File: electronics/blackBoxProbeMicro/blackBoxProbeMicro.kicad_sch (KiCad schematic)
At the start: 67 parts, among them J1 USB-C, J2 JTAG_2X05, J3 JTAG_2X05, J4 DevBoardUartOutput, Q1 BSD840N, Q2 NTJD4152P, U1 MCP1702-MB, U2 DT1446-04S, U3 STM32F103CBT, Y1 8MHz

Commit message: fixing ERC/DRC errors after component updates
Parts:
- H1, H2: symbol SquantorPCBOutline:Drill_Hole_no_metal -> Mechanical:MountingHole
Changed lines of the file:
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@@
     (stroke (width 0) (type default) (color 0 0 0 0))
   )
-  (wire (pts (xy 114.3 91.44) (xy 113.03 91.44))
+  (wire (pts (xy 110.49 91.44) (xy 114.3 91.44))
     (stroke (width 0) (type default) (color 0 0 0 0))
   )
@@
     (stroke (width 0) (type default) (color 0 0 0 0))
   )
-  (wire (pts (xy 99.06 91.44) (xy 100.33 91.44))
+  (wire (pts (xy 99.06 91.44) (xy 102.87 91.44))
     (stroke (width 0) (type default) (color 0 0 0 0))
   )
@@
     (pin "2")
   )
-  (symbol (lib_id "SquantorPCBOutline:Drill_Hole_no_metal") (at 38.1 187.96 0) (unit 1)
+  (symbol (lib_id "Mechanical:MountingHole") (at 38.1 187.96 0) (unit 1)
     (in_bom yes) (on_board yes)
     (property "Reference" "H2" (id 0) (at 42.6212 186.6138 0)
@@
     )
     (property "Footprint" "SquantorPcbOutline:MountingHole_2.5mm_no_metal" (id 2) (at 38.1 187.96 0)
-      (effects (font (size 1.524 1.524)) hide)
-    )
-    (property "Datasheet" "" (id 3) (at 38.1 187.96 0)
-      (effects (font (size 1.524 1.524)) hide)
-    )
-  )
-  (symbol (lib_id "SquantorPCBOutline:Drill_Hole_no_metal") (at 38.1 179.07 0) (unit 1)
+      (effects (font (size 1.27 1.27)) hide)
+    )
+    (property "Datasheet" "~" (id 3) (at 38.1 187.96 0)
+      (effects (font (size 1.27 1.27)) hide)
+    )
+  )
+  (symbol (lib_id "Mechanical:MountingHole") (at 38.1 179.07 0) (unit 1)
     (in_bom yes) (on_board yes)
     (property "Reference" "H1" (id 0) (at 42.6212 177.7238 0)
@@
     )
     (property "Footprint" "SquantorPcbOutline:MountingHole_2.5mm_no_metal" (id 2) (at 38.1 179.07 0)
-      (effects (font (size 1.524 1.524)) hide)
-    )
-    (property "Datasheet" "" (id 3) (at 38.1 179.07 0)
-      (effects (font (size 1.524 1.524)) hide)
-    )
-  )
+      (effects (font (size 1.27 1.27)) hide)
+    )
+    (property "Datasheet" "~" (id 3) (at 38.1 179.07 0)
+      (effects (font (size 1.27 1.27)) hide)
+    )
+  )

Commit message: small uppdates
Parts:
- N2: value V:20230224 -> V:20230929

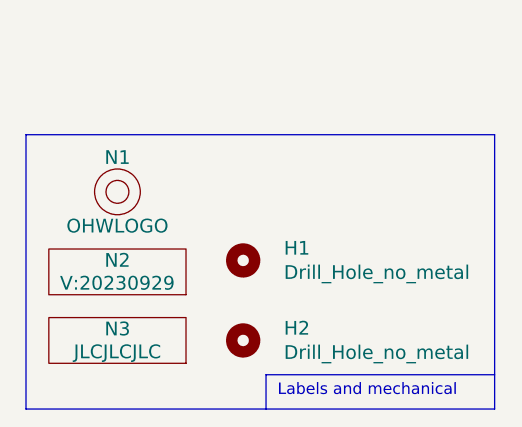
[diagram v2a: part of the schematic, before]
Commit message: WIP adapting to aisler DRC
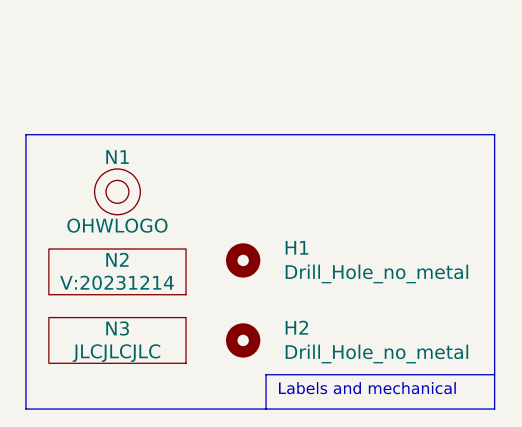
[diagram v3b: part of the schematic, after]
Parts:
- N2: value V:20230929 -> V:20231214
- U1: footprint SquantorIC:SOT89-NXP-Viatab -> SquantorIC:SOT89-NXP
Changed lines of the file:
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@@
       (effects (font (size 1.524 1.524)))
     )
-    (property "Footprint" "SquantorIC:SOT89-NXP-Viatab" (at 76.2 127 0)
+    (property "Footprint" "SquantorIC:SOT89-NXP" (at 76.2 127 0)
       (effects (font (size 1.524 1.524)) hide)
     )
@@
       (effects (font (size 1.524 1.524)))
     )
-    (property "Value" "V:20230929" (at 24.13 181.61 0)
-      (effects (font (size 1.524 1.524)))
-    )
+    (property "Value" "V:20231214" (at 24.13 181.61 0)
+      (effects (font (size 1.524 1.524)))
+    )

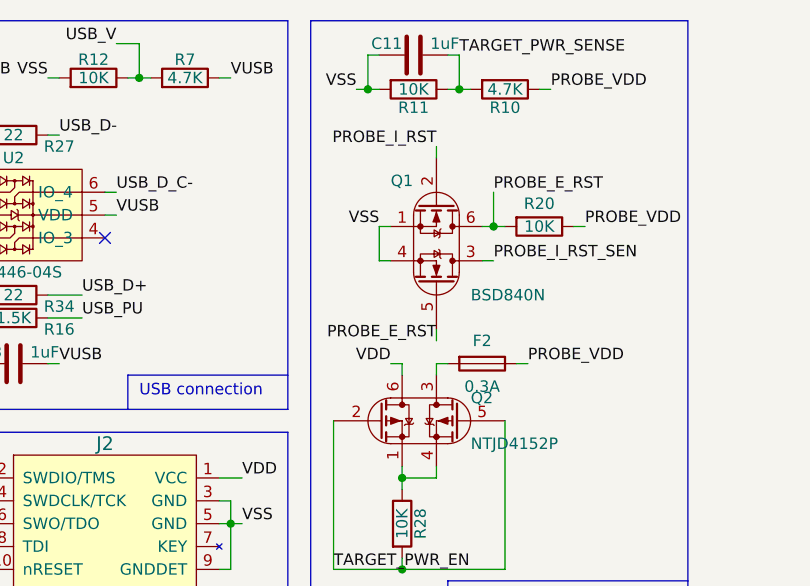
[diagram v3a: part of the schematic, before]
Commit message: WIP updating parts and PCB, replacing silk parts
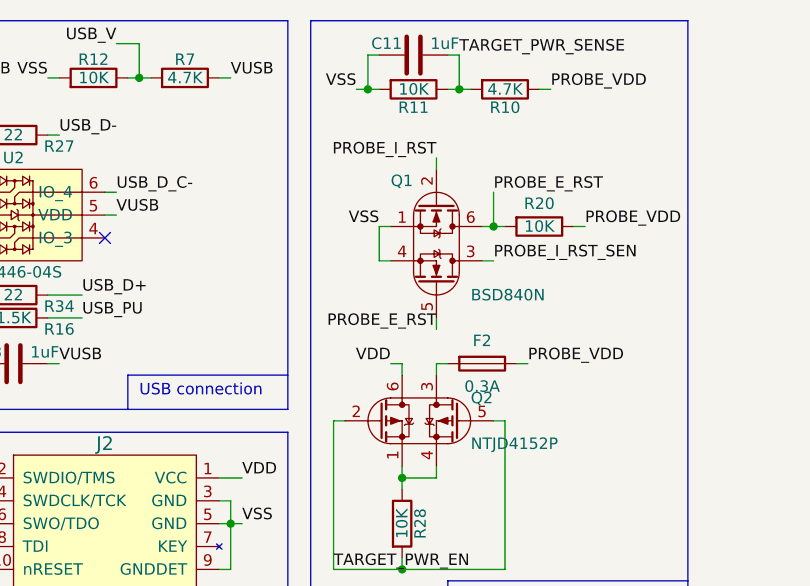
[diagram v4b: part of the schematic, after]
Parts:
- C1, C2, C4: footprint SquantorRcl:C_0603 -> SquantorCapacitor:C_0603
- C10, C11, C12, C13, C3, C5, C6, C7, C8: footprint SquantorRcl:C_0402 -> SquantorCapacitor:C_0402
- F1, F2: footprint SquantorRcl:F_0603_hand -> SquantorFuse:F_0603_hand
- FB1: footprint SquantorRcl:L_0603 -> SquantorInductor:L_0603
- FB2, FB3: footprint SquantorRcl:L_0402 -> SquantorInductor:L_0402
- J4: footprint Connector_JST:JST_PH_S4B-PH-K_1x04_P2.00mm_Horizontal -> SquantorConnectors:JST_PH_S4B-PH-K_1x04_P2.00mm_Horizontal
- R1, R10, R11, R12, R13, R14, R15, R16, R17, R18, R19, R2, R20, R21, R22, R23, R24, R25, R27, R28, R3, R34, R4, R5, R6, R7, R8, R9: footprint SquantorRcl:R_0402_hand -> SquantorResistor:R_0402_hand

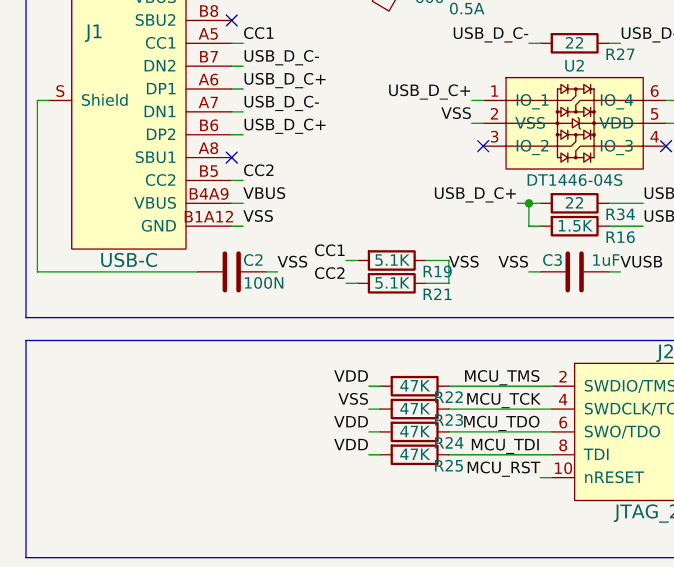
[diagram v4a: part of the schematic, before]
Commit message: WIP relayout on new DRC rules
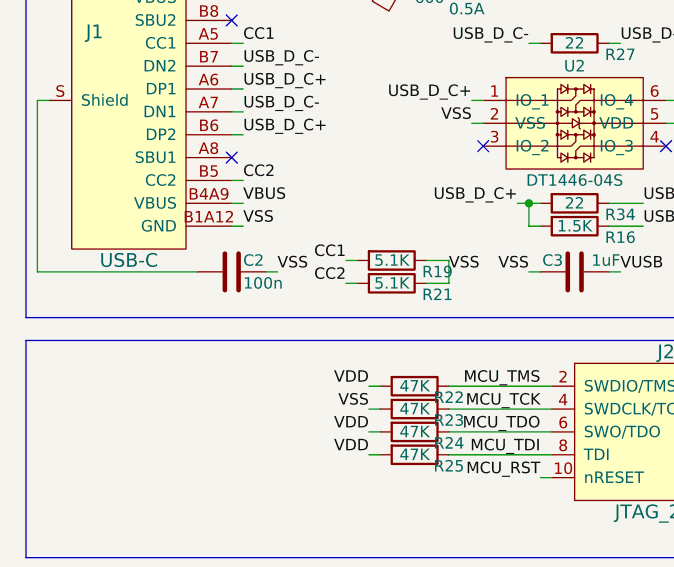
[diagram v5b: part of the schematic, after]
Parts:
- C2: value 100N -> 100n
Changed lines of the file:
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@@
       (effects (font (size 1.27 1.27)) (justify left))
     )
-    (property "Value" "100N" (at 38.1 53.34 90)
+    (property "Value" "100n" (at 38.1 53.34 90)
       (effects (font (size 1.27 1.27)) (justify left))
     )

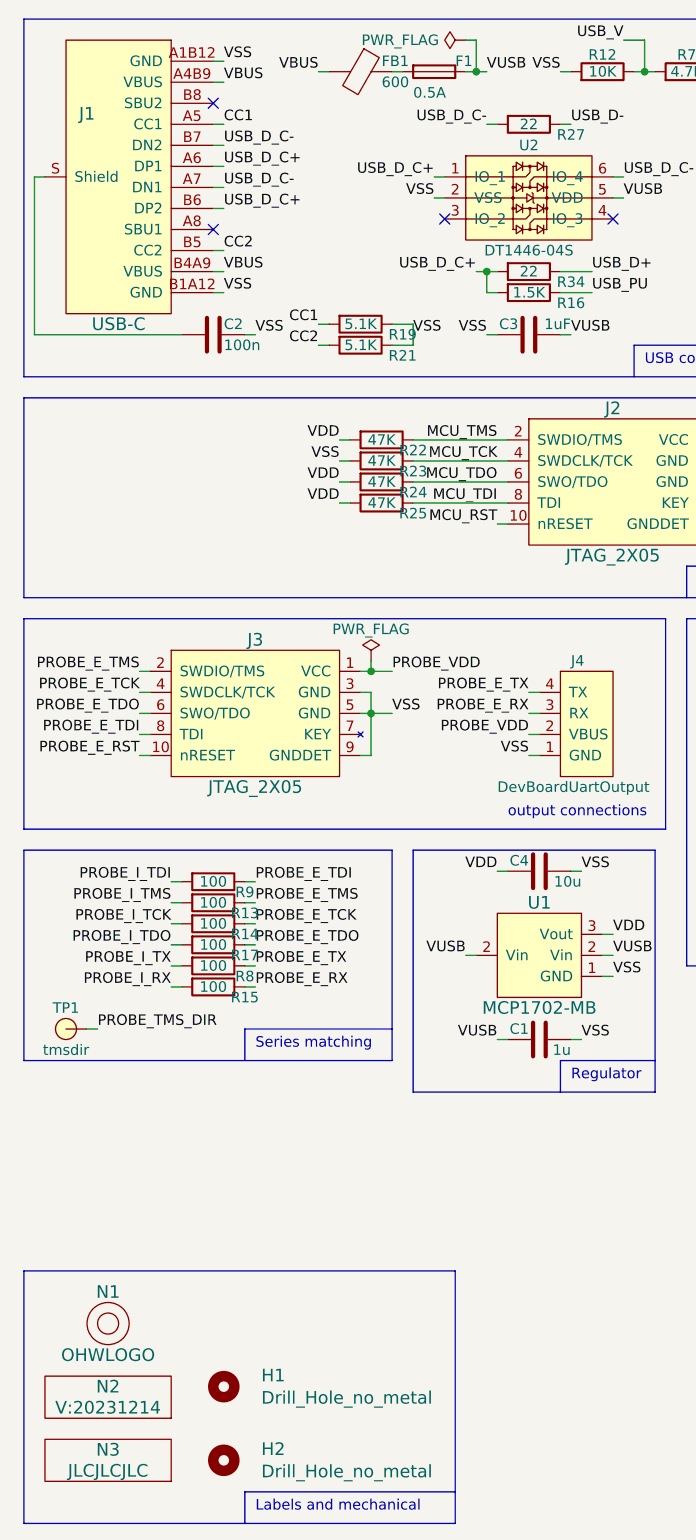
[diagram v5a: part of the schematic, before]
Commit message: adjustments of silk, fixing ERC errors
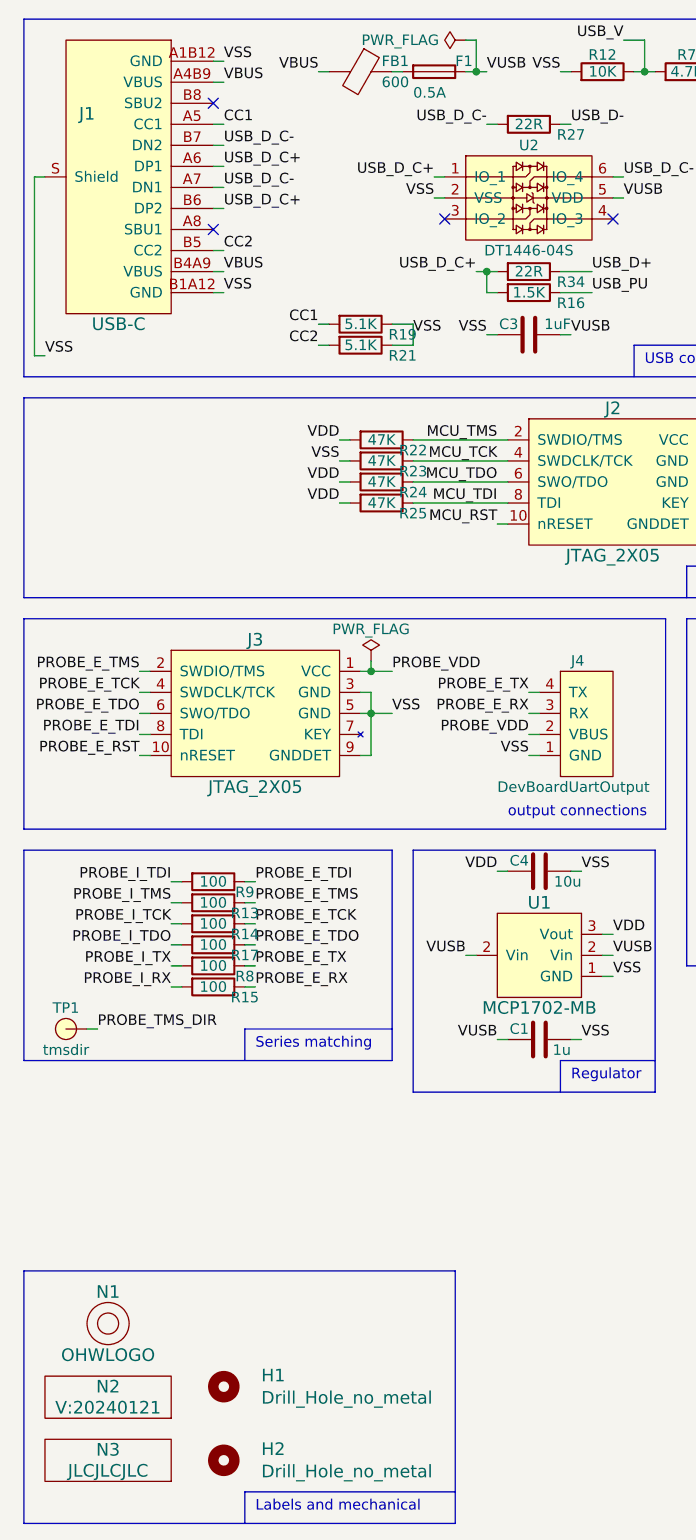
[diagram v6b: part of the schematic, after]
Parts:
- removed C2: 100n, SquantorCapacitor:C_0603, symbol Device:C
- N2: value V:20231214 -> V:20240121
- R27, R34: value 22 -> 22R
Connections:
- net VSS: now also J1.S (Shield)
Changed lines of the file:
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@@
-    (stroke (width 0) (type default))
-  )
-  (wire (pts (xy 33.02 52.07) (xy 15.24 52.07))
     (stroke (width 0) (type default))
   )
@@
     (stroke (width 0) (type default))
   )
-  (wire (pts (xy 15.24 52.07) (xy 15.24 33.02))
-    (stroke (width 0) (type default))
-  )
   (wire (pts (xy 227.33 39.37) (xy 226.06 39.37))
     (stroke (width 0) (type default))
@@
     (stroke (width 0) (type default))
   )
+  (wire (pts (xy 15.24 33.02) (xy 15.24 54.61))
+    (stroke (width 0) (type default))
+  )
   (polyline (pts (xy 105.41 59.69) (xy 105.41 83.82))
     (stroke (width 0) (type default))
@@
     (stroke (width 0) (type default))
   )
-  (wire (pts (xy 15.24 33.02) (xy 16.51 33.02))
-    (stroke (width 0) (type default))
-  )
   (wire (pts (xy 115.57 40.64) (xy 116.84 40.64))
     (stroke (width 0) (type default))
@@
     (stroke (width 0) (type default))
   )
-  (wire (pts (xy 40.64 52.07) (xy 41.91 52.07))
-    (stroke (width 0) (type default))
-  )
   (polyline (pts (xy 175.26 166.37) (xy 175.26 195.58))
     (stroke (width 0) (type default))
@@
     (stroke (width 0) (type default))
   )
+  (wire (pts (xy 16.51 33.02) (xy 15.24 33.02))
+    (stroke (width 0) (type default))
+  )
   (wire (pts (xy 72.39 74.93) (xy 71.12 74.93))
     (stroke (width 0) (type default))
@@
     (stroke (width 0) (type default))
   )
+  (wire (pts (xy 15.24 54.61) (xy 16.51 54.61))
+    (stroke (width 0) (type default))
+  )
   (polyline (pts (xy 184.15 160.02) (xy 283.21 160.02))
     (stroke (width 0) (type default))
@@
     (effects (font (size 1.27 1.27)) (justify right bottom))
   )
-  (label "VSS" (at 41.91 52.07 0) (fields_autoplaced)
+  (label "VSS" (at 16.51 54.61 0) (fields_autoplaced)
     (effects (font (size 1.27 1.27)) (justify left bottom))
   )
@@
         (path "/40f15b6a-8b98-4774-8d8e-1b991685cf13"
           (reference "J1") (unit 1)
-        )
-      )
-    )
-  )
-  (symbol (lib_id "Device:C") (at 36.83 52.07 270) (unit 1)
-    (in_bom yes) (on_board yes) (dnp no)
-    (property "Reference" "C2" (at 38.1 50.8 90)
-      (effects (font (size 1.27 1.27)) (justify left))
-    )
-    (property "Value" "100n" (at 38.1 53.34 90)
-      (effects (font (size 1.27 1.27)) (justify left))
-    )
-    (property "Footprint" "SquantorCapacitor:C_0603" (at 33.02 53.0352 0)
-      (effects (font (size 1.27 1.27)) hide)
-    )
-    (property "Datasheet" "~" (at 36.83 52.07 0)
-      (effects (font (size 1.27 1.27)) hide)
-    )
-    (pin "1")
-    (pin "2")
-    (instances
-      (project "blackBoxProbeMicro"
-        (path "/40f15b6a-8b98-4774-8d8e-1b991685cf13"
-          (reference "C2") (unit 1)
         )
       )
@@
       (effects (font (size 1.27 1.27)))
     )
-    (property "Value" "22" (at 74.93 26.67 90)
+    (property "Value" "22R" (at 74.93 26.67 90)
       (effects (font (size 1.27 1.27)))
     )
@@
       (effects (font (size 1.27 1.27)))
     )
-    (property "Value" "22" (at 74.93 44.45 90)
+    (property "Value" "22R" (at 74.93 44.45 90)
       (effects (font (size 1.27 1.27)))
     )
@@
       (effects (font (size 1.524 1.524)))
     )
-    (property "Value" "V:20231214" (at 24.13 181.61 0)
+    (property "Value" "V:20240121" (at 24.13 181.61 0)
       (effects (font (size 1.524 1.524)))
     )

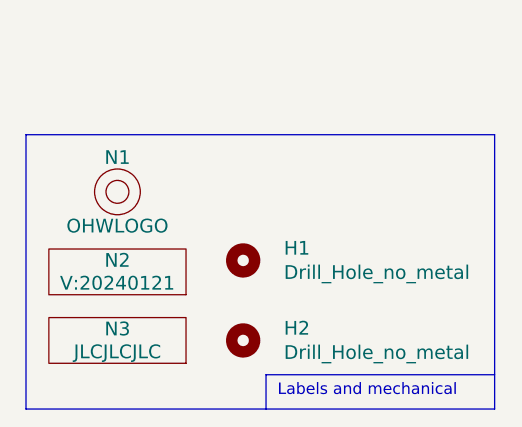
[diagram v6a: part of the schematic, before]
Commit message: all planes are now VSS planes, some routing improvements
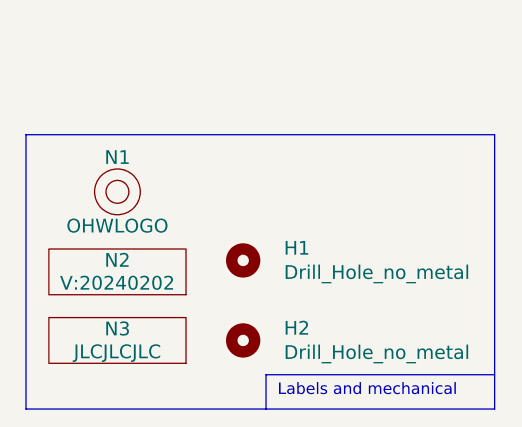
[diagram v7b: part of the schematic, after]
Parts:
- N2: value V:20240121 -> V:20240202
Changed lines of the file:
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@@
       (effects (font (size 1.524 1.524)))
     )
-    (property "Value" "V:20240121" (at 24.13 181.61 0)
+    (property "Value" "V:20240202" (at 24.13 181.61 0)
       (effects (font (size 1.524 1.524)))
     )

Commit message: reviewed and ready for production
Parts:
- N2: value V:20240202 -> V:20240216
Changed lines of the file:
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@@
       (effects (font (size 1.524 1.524)))
     )
-    (property "Value" "V:20240202" (at 24.13 181.61 0)
+    (property "Value" "V:20240216" (at 24.13 181.61 0)
       (effects (font (size 1.524 1.524)))
     )
